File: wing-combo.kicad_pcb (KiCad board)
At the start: 2 copper layers, 93 x 91.3 mm, 114 parts, among them J1 Screw_Terminal_01x06, J13 USB_A, J15 Conn_01x16, J16 Conn_01x16, J17 Screw_Terminal_01x06, J18 Screw_Terminal_01x06, J3 Conn_01x12, J4 Conn_01x12, T1 AO3400A, T2 AO3400A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

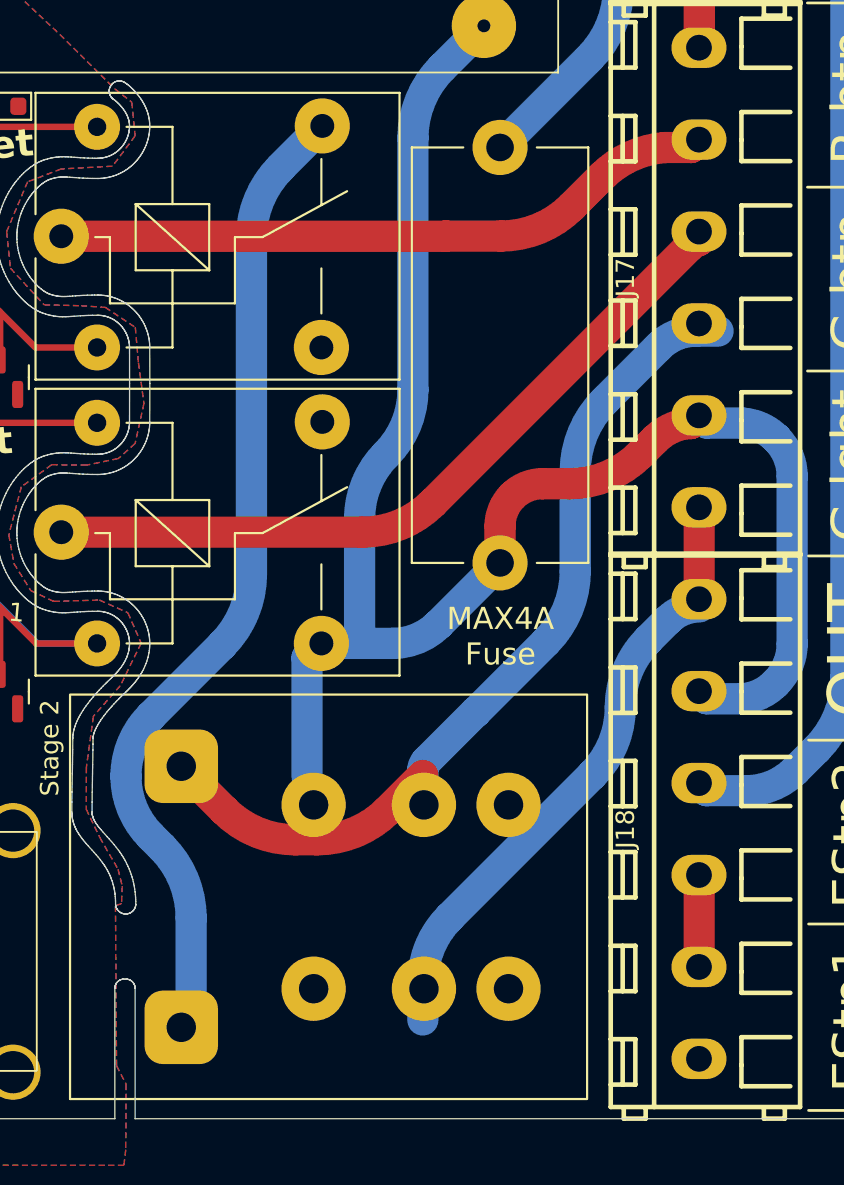
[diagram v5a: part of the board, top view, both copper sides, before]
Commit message: flipped arbitrary pin-numberrs on relay, for better routing
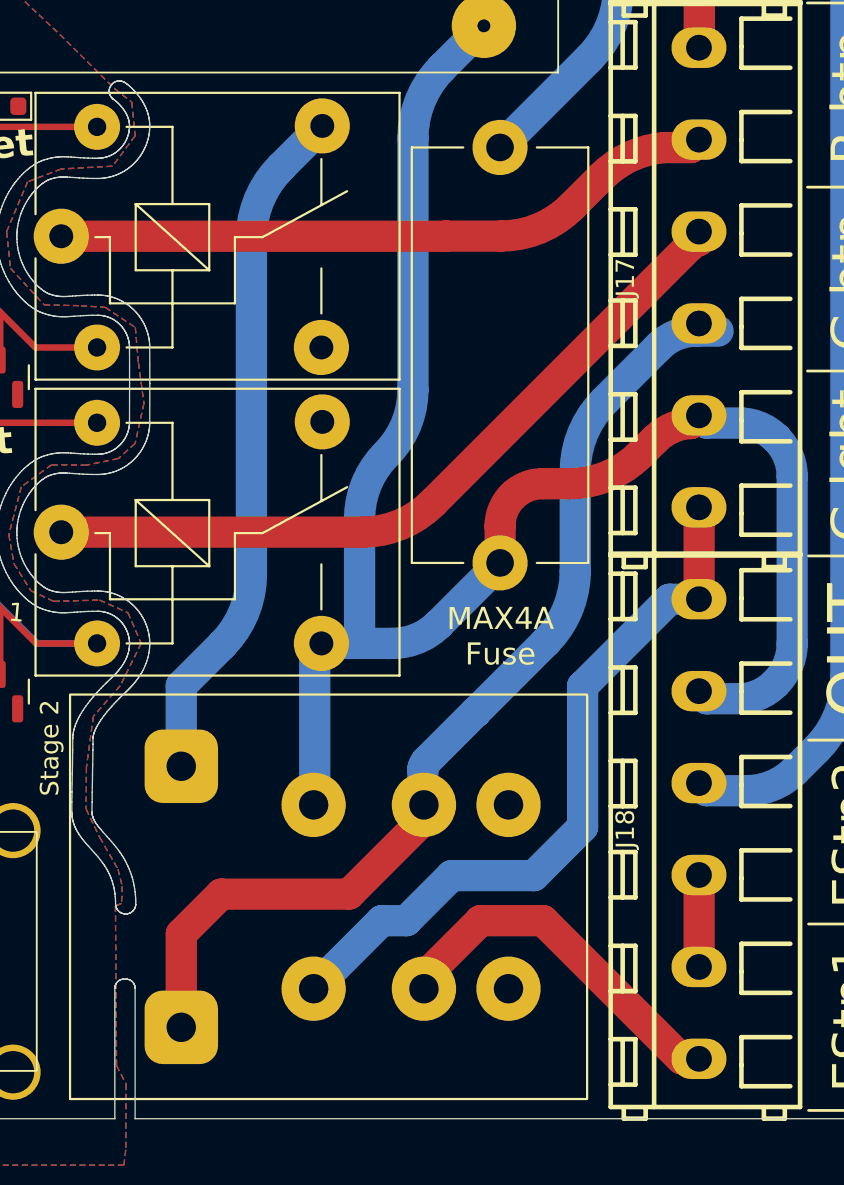
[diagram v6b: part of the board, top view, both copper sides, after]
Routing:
- net Member-E-Stop-sw1-1: track 0.00 -> 20.0 mm
- net reset: track 53.3 -> 37.5 mm
- net Member-Green-Button-2: track 46.6 -> 54.9 mm
- net Green-Indicator-light-2: track 33.4 -> 39.2 mm
- net Green-Indicator-light-1: track 93.3 -> 94.7 mm
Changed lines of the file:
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@@
 		)
 		(pad "1" thru_hole circle
-			(at -5 7.6 90)
+			(at 5 7.6 90)
 			(size 3.5 3.5)
 			(drill 1.6)
@@
 		)
 		(pad "4" thru_hole circle
-			(at 5 7.6 90)
+			(at -5 7.6 90)
 			(size 3.5 3.5)
 			(drill 1.6)
@@
 		)
 		(pad "5" thru_hole circle
-			(at -5 3 90)
+			(at 5 3 90)
 			(size 3.5 3.5)
 			(drill 1.6)
@@
 		)
 		(pad "8" thru_hole circle
-			(at 5 -3 90)
+			(at -5 -3 90)
 			(size 3.5 3.5)
 			(drill 1.6)
-			(layers "*.Cu" "*.Mask")
+			(layers "*.Cu" "*.Mask" "B.SilkS")
 			(remove_unused_layers no)
 			(net 70 "Green-Indicator-light-2")
@@
 		)
 		(pad "9" thru_hole circle
-			(at -5 -3 90)
+			(at 5 -3 90)
 			(size 3.5 3.5)
 			(drill 1.6)
-			(layers "*.Cu" "*.Mask" "B.SilkS")
+			(layers "*.Cu" "*.Mask")
 			(remove_unused_layers no)
 			(net 46 "Green-Indicator-light-1")
@@
 		)
 		(pad "12" thru_hole circle
-			(at 5 3 90)
+			(at -5 3 90)
 			(size 3.5 3.5)
 			(drill 1.6)
@@
 	)
 	(segment
-		(start 100.108792 97.406207)
-		(end 102.015 95.5)
+		(start 102.075 97.1)
+		(end 102.075 97.89)
 		(width 1.7)
 		(layer "F.Cu")
@@
 	)
 	(segment
-		(start 91.221207 97.406207)
-		(end 89.315 95.5)
+		(start 88.875 104.12)
+		(end 88.875 109.2)
 		(width 1.7)
 		(layer "F.Cu")
@@
 	)
 	(segment
-		(start 95.068963 99)
-		(end 96.261036 99)
+		(start 98.015 101.95)
+		(end 91.045 101.95)
 		(width 1.7)
 		(layer "F.Cu")
 		(net 7)
 	)
-	(arc
-		(start 91.221207 97.406207)
-		(mid 92.986572 98.585786)
-		(end 95.068963 99)
+	(segment
+		(start 102.075 97.89)
+		(end 98.015 101.95)
 		(width 1.7)
 		(layer "F.Cu")
 		(net 7)
 	)
-	(arc
-		(start 100.108792 97.406207)
-		(mid 98.343426 98.585786)
-		(end 96.261036 99)
+	(segment
+		(start 91.045 101.95)
+		(end 88.875 104.12)
 		(width 1.7)
 		(layer "F.Cu")
@@
 	)
 	(segment
-		(start 110.305 78.973963)
-		(end 110.305 84.386036)
+		(start 104.882767 92.053195)
+		(end 102.21972 94.716242)
 		(width 1.7)
 		(layer "B.Cu")
@@
 	)
 	(segment
-		(start 116.885 71.33)
-		(end 118.075 71.33)
+		(start 108.711207 88.233792)
+		(end 104.898195 92.046804)
 		(width 1.7)
 		(layer "B.Cu")
@@
 	)
 	(segment
-		(start 111.898792 75.126207)
-		(end 114.853542 72.171457)
+		(start 102.014766 97.039766)
+		(end 102.075 97.1)
 		(width 1.7)
 		(layer "B.Cu")
@@
 	)
 	(segment
-		(start 102.015 95.210481)
-		(end 102.015 95.5)
+		(start 89.3891 108.7759)
+		(end 89.365 108.8)
 		(width 1.7)
 		(layer "B.Cu")
@@
 	)
 	(segment
-		(start 108.711207 88.233792)
-		(end 104.898195 92.046804)
+		(start 110.305 78.973963)
+		(end 110.305 84.386036)
 		(width 1.7)
 		(layer "B.Cu")
@@
 	)
 	(segment
-		(start 102.21972 94.716242)
+		(start 104.890481 92.05)
 		(end 104.882767 92.053195)
 		(width 1.7)
@@
 		(net 7)
 	)
-	(arc
+	(segment
 		(start 104.898195 92.046804)
-		(mid 104.894655 92.049169)
 		(end 104.890481 92.05)
 		(width 1.7)
@@
 		(net 7)
 	)
-	(arc
-		(start 116.885 71.33)
-		(mid 115.785583 71.548687)
-		(end 114.853542 72.171457)
+	(segment
+		(start 102.014766 95.155453)
+		(end 102.014766 97.039766)
+		(width 1.7)
+		(layer "B.Cu")
+		(net 7)
+	)
+	(segment
+		(start 114.853542 72.171457)
+		(end 111.898792 75.126207)
+		(width 1.7)
+		(layer "B.Cu")
+		(net 7)
+	)
+	(segment
+		(start 118.075 71.33)
+		(end 116.885 71.33)
 		(width 1.7)
 		(layer "B.Cu")
@@
 	)
 	(arc
-		(start 110.305 84.386036)
-		(mid 109.890786 86.468426)
-		(end 108.711207 88.233792)
+		(start 102.21972 94.716242)
+		(mid 102.079206 94.917856)
+		(end 102.014766 95.155453)
 		(width 1.7)
 		(layer "B.Cu")
@@
 	)
 	(arc
-		(start 104.890481 92.05)
-		(mid 104.886306 92.05083)
-		(end 104.882767 92.053195)
+		(start 116.885 71.33)
+		(mid 115.785583 71.548687)
+		(end 114.853542 72.171457)
 		(width 1.7)
 		(layer "B.Cu")
@@
 	)
 	(arc
-		(start 102.21972 94.716242)
-		(mid 102.068204 94.943001)
-		(end 102.015 95.210481)
+		(start 89.4132 108.717717)
+		(mid 89.406936 108.749205)
+		(end 89.3891 108.7759)
+		(width 1.7)
+		(layer "B.Cu")
+		(net 7)
+	)
+	(arc
+		(start 110.305 84.386036)
+		(mid 109.890786 86.468426)
+		(end 108.711207 88.233792)
 		(width 1.7)
 		(layer "B.Cu")
@@
 	)
 	(segment
+		(start 96.135 88.6792)
+		(end 96.4966 88.3176)
+		(width 1.7)
+		(layer "B.Cu")
+		(net 46)
+	)
+	(segment
+		(start 96.135 97.04)
+		(end 96.135 88.6792)
+		(width 1.7)
+		(layer "B.Cu")
+		(net 46)
+	)
+	(segment
 		(start 99.142442 88.3176)
 		(end 100.3724 88.3176)
@@
 	)
 	(segment
-		(start 95.715 95.55)
-		(end 95.715 89.0992)
-		(width 1.7)
-		(layer "B.Cu")
-		(net 46)
-	)
-	(segment
 		(start 98.575 87.750157)
 		(end 98.575 81.530609)
@@
 	)
 	(segment
-		(start 95.715 89.0992)
-		(end 96.4966 88.3176)
+		(start 103.068792 56.994407)
+		(end 105.3366 54.7266)
 		(width 1.7)
 		(layer "B.Cu")
@@
 	)
 	(segment
-		(start 103.068792 56.994407)
-		(end 105.3366 54.7266)
+		(start 96.075 97.1)
+		(end 96.135 97.04)
 		(width 1.7)
 		(layer "B.Cu")
@@
 	)
 	(segment
+		(start 105.142409 103.4)
+		(end 108.565 103.4)
+		(width 1.7)
+		(layer "F.Cu")
+		(net 60)
+	)
+	(segment
+		(start 102.075 106.467409)
+		(end 105.142409 103.4)
+		(width 1.7)
+		(layer "F.Cu")
+		(net 60)
+	)
+	(segment
+		(start 102.075 107.1)
+		(end 102.075 106.467409)
+		(width 1.7)
+		(layer "F.Cu")
+		(net 60)
+	)
+	(segment
+		(start 108.565 103.4)
+		(end 116.08 110.915)
+		(width 1.7)
+		(layer "F.Cu")
+		(net 60)
+	)
+	(segment
+		(start 116.08 110.915)
+		(end 117.035 110.915)
+		(width 1.7)
+		(layer "F.Cu")
+		(net 60)
+	)
+	(segment
 		(start 54.800293 82.840993)
 		(end 54.810007 82.840993)
@@
 	)
 	(segment
-		(start 111.23506 95.458976)
-		(end 103.47198 103.222056)
+		(start 103.575 100.95)
+		(end 101.125 103.4)
 		(width 1.7)
 		(layer "B.Cu")
@@
 	)
 	(segment
-		(start 102.015 106.739518)
-		(end 102.015 108.8)
+		(start 101.125 103.4)
+		(end 99.775 103.4)
 		(width 1.7)
 		(layer "B.Cu")
@@
 	)
 	(segment
-		(start 114.274938 88.12006)
-		(end 115.354357 87.040642)
+		(start 110.705 90.64)
+		(end 110.705 98.302591)
 		(width 1.7)
 		(layer "B.Cu")
 		(net 70)
 	)
-	(arc
-		(start 112.755 91.789518)
-		(mid 112.35998 93.775414)
-		(end 111.23506 95.458976)
+	(segment
+		(start 99.775 103.4)
+		(end 96.075 107.1)
 		(width 1.7)
 		(layer "B.Cu")
 		(net 70)
 	)
-	(arc
-		(start 103.47198 103.222056)
-		(mid 102.393656 104.835881)
-		(end 102.015 106.739518)
+	(segment
+		(start 110.705 98.302591)
+		(end 108.057591 100.95)
 		(width 1.7)
 		(layer "B.Cu")
 		(net 70)
 	)
-	(arc
-		(start 117.07 86.33)
-		(mid 116.1415 86.514689)
-		(end 115.354357 87.040642)
+	(segment
+		(start 115.43 85.915)
+		(end 110.705 90.64)
 		(width 1.7)
 		(layer "B.Cu")
 		(net 70)
 	)
-	(arc
-		(start 114.274938 88.12006)
-		(mid 113.150019 89.803621)
-		(end 112.755 91.789518)
+	(segment
+		(start 108.057591 100.95)
+		(end 103.575 100.95)
 		(width 1.7)
 		(layer "B.Cu")
@@
 	)
 	(segment
-		(start 89.4132 103.252163)
-		(end 89.4132 108.717717)
+		(start 117.035 85.915)
+		(end 115.43 85.915)
 		(width 1.7)
 		(layer "B.Cu")
-		(net 71)
+		(net 70)
 	)
 	(segment
@@
 	)
 	(segment
-		(start 87.819407 99.404407)
-		(end 87.215 98.8)
-		(width 1.7)
-		(layer "B.Cu")
-		(net 71)
-	)
-	(segment
-		(start 94.286792 62.429607)
-		(end 96.5466 60.1698)
+		(start 91.099207 88.397415)
+		(end 88.875 90.621622)
 		(width 1.7)
 		(layer "B.Cu")
@@
 	)
 	(segment
-		(start 91.099207 88.397415)
-		(end 87.215 92.281622)
+		(start 96.5466 60.1698)
+		(end 94.286792 62.429607)
 		(width 1.7)
 		(layer "B.Cu")
@@
 	)
 	(segment
-		(start 89.3891 108.7759)
-		(end 89.365 108.8)
+		(start 88.875 90.621622)
+		(end 88.875 95)
 		(width 1.7)
 		(layer "B.Cu")
@@
 		(width 1.7)
 		(layer "B.Cu")
-		(net 71)
-	)
-	(arc
-		(start 87.215 92.281622)
-		(mid 86.215853 93.77695)
-		(end 85.865 95.540811)
-		(width 1.7)
-		(layer "B.Cu")
-		(net 71)
-	)
-	(arc
-		(start 87.819407 99.404407)
-		(mid 88.998986 101.169772)
-		(end 89.4132 103.252163)
-		(width 1.7)
-		(layer "B.Cu")
-		(net 71)
-	)
-	(arc
-		(start 89.4132 108.717717)
-		(mid 89.406936 108.749205)
-		(end 89.3891 108.7759)
-		(width 1.7)
-		(layer "B.Cu")
-		(net 71)
-	)
-	(arc
-		(start 85.865 95.540811)
-		(mid 86.215853 97.304671)
-		(end 87.215 98.8)
-		(width 1.7)
-		(layer "B.Cu")
